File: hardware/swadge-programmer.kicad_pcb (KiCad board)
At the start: 2 copper layers, 73.7 x 73.7 mm, 28 parts, among them J1 USB_B_Micro, J2 Conn_02x21_Top_Bottom, J3 Conn_02x21_Top_Bottom, J4 ftdi-header, J5 Conn_01x03_Male, SW1 4-1437565-2, SW2 4-1437565-2, SW3 4-1437565-2, SW4 SW_DPDT_x2, SW5 SW_DPDT_x2, U1 BUS_PCIexpress, U2 CP2102N-A01-GQFN24

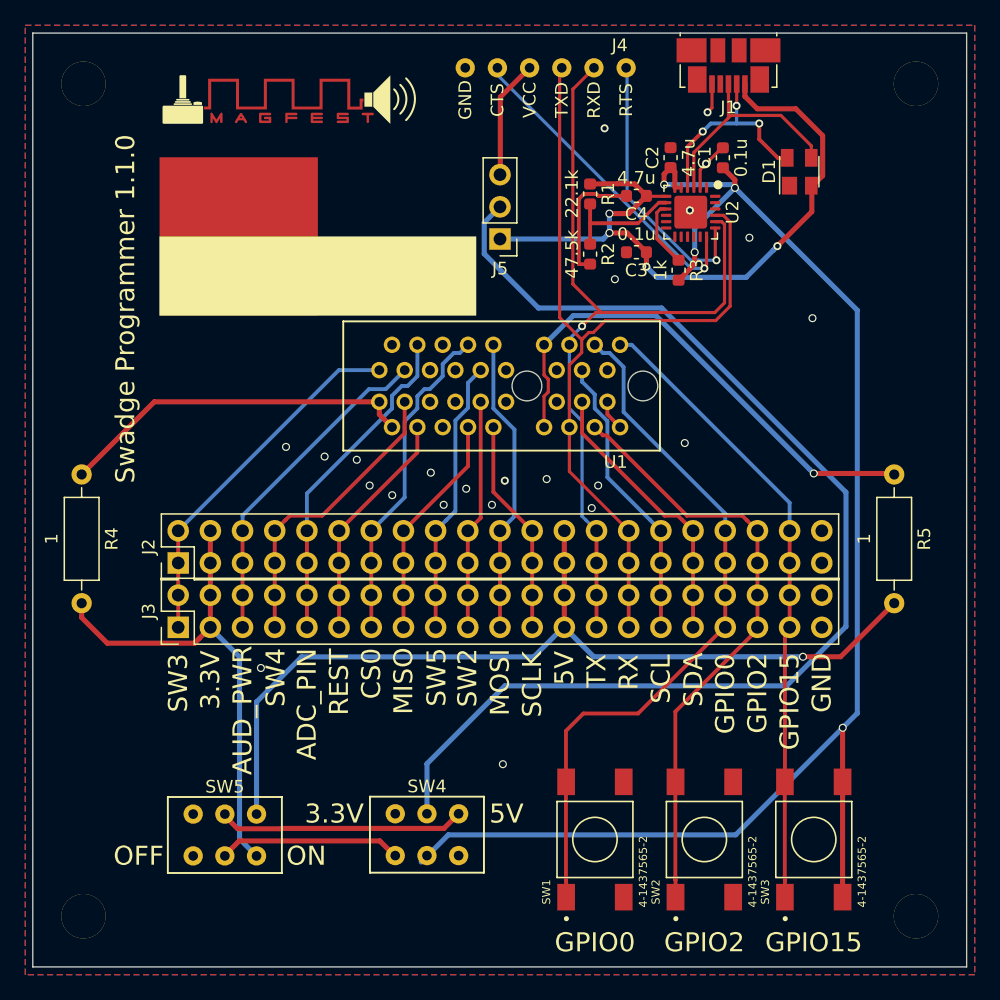
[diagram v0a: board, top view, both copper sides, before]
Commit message: #17 Reordered PCIe connector on programmer
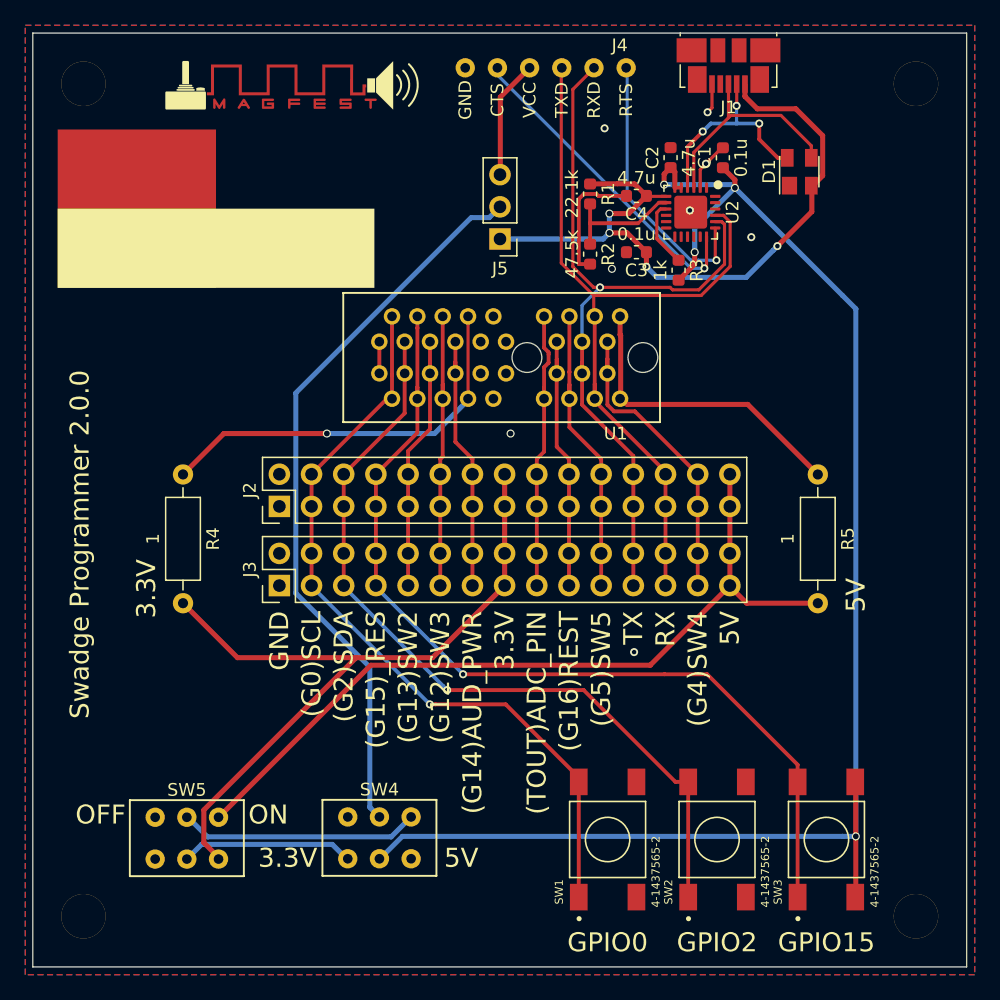
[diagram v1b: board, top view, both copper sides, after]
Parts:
- J2, J3: value Conn_02x21_Top_Bottom -> Conn_02x15_Top_Bottom; footprint Swadge_Parts:PinHeader_2x21_P2.54mm_Vertical -> Swadge_Parts:PinHeader_2x15_P2.54mm_Vertical
- moved J2 9.15 mm to (128.0, 87.5)
- moved J3 8.64 mm to (128.0, 93.8)
- moved svg2mod 8.33 mm to (123.0, 64.0)
- moved R4 8.00 mm to (120.4, 85.0)
- moved R5 6.03 mm to (170.5, 85.0)
- moved SW4 3.76 mm to (135.9, 113.7)
- moved SW5 3.01 mm to (120.7, 113.7)
- moved U1 2.25 mm to (147.5, 75.8)
- moved svg2mod 1.14 mm to (129.0, 54.2)
- moved SW1 1.00 mm to (153.9, 113.8)
- moved SW2 1.00 mm to (162.5, 113.8)
- moved SW3 1.00 mm to (171.2, 113.8)
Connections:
- J2 pad 1: SW3 -> GND
- J2 pad 10: ADC_PIN -> SW2
- J2 pad 11: REST -> SW3
- J2 pad 12: REST -> SW3
- J2 pad 13: CS0 -> AUD_PWR
- J2 pad 14: CS0 -> AUD_PWR
- J2 pad 15: MISO -> 3.3V
- J2 pad 16: MISO -> 3.3V
- J2 pad 17: SW5 -> ADC_PIN
- J2 pad 18: SW5 -> ADC_PIN
- J2 pad 19: SW2 -> REST
- J2 pad 2: SW3 -> GND
- J2 pad 20: SW2 -> REST
- J2 pad 21: MOSI -> SW5
- J2 pad 22: MOSI -> SW5
- J2 pad 23: SCLK -> TX
- J2 pad 24: SCLK -> TX
- J2 pad 25: 5V -> RX
- J2 pad 26: 5V -> RX
- J2 pad 27: TX -> SW4
- J2 pad 28: TX -> SW4
- J2 pad 29: RX -> 5V
- J2 pad 3: 3.3V -> SCL
- J2 pad 30: RX -> 5V
- J2 pad 4: 3.3V -> SCL
- J2 pad 5: AUD_PWR -> SDA
- J2 pad 6: AUD_PWR -> SDA
- J2 pad 7: SW4 -> _RES
- J2 pad 8: SW4 -> _RES
- J2 pad 9: ADC_PIN -> SW2
- J3 pad 1: SW3 -> GND
- J3 pad 10: ADC_PIN -> SW2
- J3 pad 11: REST -> SW3
- J3 pad 12: REST -> SW3
- J3 pad 13: CS0 -> AUD_PWR
- J3 pad 14: CS0 -> AUD_PWR
- J3 pad 15: MISO -> 3.3V
- J3 pad 16: MISO -> 3.3V
- J3 pad 17: SW5 -> ADC_PIN
- J3 pad 18: SW5 -> ADC_PIN
- J3 pad 19: SW2 -> REST
- J3 pad 2: SW3 -> GND
- J3 pad 20: SW2 -> REST
- J3 pad 21: MOSI -> SW5
- J3 pad 22: MOSI -> SW5
- J3 pad 23: SCLK -> TX
- J3 pad 24: SCLK -> TX
- J3 pad 25: 5V -> RX
- J3 pad 26: 5V -> RX
- J3 pad 27: TX -> SW4
- J3 pad 28: TX -> SW4
- J3 pad 29: RX -> 5V
- J3 pad 3: 3.3V -> SCL
- J3 pad 30: RX -> 5V
- J3 pad 4: 3.3V -> SCL
- J3 pad 5: AUD_PWR -> SDA
- J3 pad 6: AUD_PWR -> SDA
- J3 pad 7: SW4 -> _RES
- J3 pad 8: SW4 -> _RES
- J3 pad 9: ADC_PIN -> SW2
- SW1 pad 1: GPIO0 -> SCL
- SW1 pad 2: GPIO0 -> SCL
- SW2 pad 1: GPIO2 -> SDA
- SW2 pad 2: GPIO2 -> SDA
- SW3 pad 1: GPIO15 -> _RES
- SW3 pad 2: GPIO15 -> _RES
- U1 pad A1: SW3 -> GND
- U1 pad A10: MOSI -> (no net)
- U1 pad A12: Net-(R5-Pad1) -> ADC_PIN
- U1 pad A13: (no net) -> REST
- U1 pad A14: TX -> SW5
- U1 pad A15: SCL -> TX
- U1 pad A16: GPIO0 -> RX
- U1 pad A17: (no net) -> SW4
- U1 pad A18: GPIO15 -> Net-(R5-Pad1)
- U1 pad A2: (no net) -> SCL
- U1 pad A3: AUD_PWR -> SDA
- U1 pad A4: ADC_PIN -> _RES
- U1 pad A5: (no net) -> SW2
- U1 pad A6: (no net) -> SW3
- U1 pad A7: (no net) -> AUD_PWR
- U1 pad A8: CS0 -> Net-(R4-Pad1)
- U1 pad A9: SW5 -> (no net)
- U1 pad B1: Net-(R4-Pad1) -> GND
- U1 pad B10: SCLK -> (no net)
- U1 pad B12: Net-(R5-Pad1) -> ADC_PIN
- U1 pad B13: (no net) -> REST
- U1 pad B14: RX -> SW5
- U1 pad B15: SDA -> TX
- U1 pad B16: GPIO2 -> RX
- U1 pad B17: GND -> SW4
- U1 pad B18: GND -> Net-(R5-Pad1)
- U1 pad B2: Net-(R4-Pad1) -> SCL
- U1 pad B3: SW4 -> SDA
- U1 pad B4: REST -> _RES
- U1 pad B5: (no net) -> SW2
- U1 pad B6: (no net) -> SW3
- U1 pad B7: (no net) -> AUD_PWR
- U1 pad B8: MISO -> Net-(R4-Pad1)
- U1 pad B9: SW2 -> (no net)
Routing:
- net _RES: track 0.00 -> 73.5 mm, vias 0 -> 1
- net GPIO0: track 55.8 -> 0.00 mm
- net GPIO15: track 49.7 -> 0.00 mm
- net GPIO2: track 48.0 -> 0.00 mm
- net SDA: track 22.1 -> 64.1 mm, vias 0 -> 1
- net SCL: track 22.9 -> 61.1 mm, vias 0 -> 1
- net +5V: track 92.7 -> 58.4 mm
- net CS0: track 26.0 -> 0.00 mm
- net MOSI: track 23.5 -> 0.00 mm
- net 3.3V: track 39.9 -> 59.4 mm
- net MISO: track 17.9 -> 0.00 mm
- net SCLK: track 17.1 -> 0.00 mm
- net Net-(R5-Pad1): track 40.5 -> 24.6 mm, vias 1 -> 0
- net 5V: track 71.8 -> 64.3 mm, vias 1 -> 0
- net SW3: track 28.7 -> 22.5 mm
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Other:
- board text added: "(G0)SCL"
- board text added: "(G12)SW3"
- board text added: "(G13)SW2"
- board text added: "(G14)AUD_PWR"
- board text added: "(G15)_RES"
- board text added: "(G16)REST"
- board text added: "(G2)SDA"
- board text added: "(G4)SW4"
- board text added: "(G5)SW5"
- board text added: "(TOUT)ADC_PIN"
- board text added: "Swadge Programmer 2.0.0"
- board text removed: "ADC_PIN"
- board text removed: "AUD_PWR"
- board text removed: "CS0"
- board text removed: "MISO"
- board text removed: "MOSI"
- board text removed: "REST"
- board text removed: "SCL"
- board text removed: "SCLK"
- board text removed: "SDA"
- board text removed: "SW2"
- board text removed: "SW3"
- board text removed: "SW4"
- board text removed: "SW5"
- board text removed: "Swadge Programmer 1.1.0"
